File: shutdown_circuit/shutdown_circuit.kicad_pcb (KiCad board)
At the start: 2 copper layers, 36.8 x 25.8 mm, 21 parts, among them J1 SFTY, M3 Mounting_Hole, U1 AP111750, U2 74HC20D, U3 BTS6133D, m3 Mounting_Hole

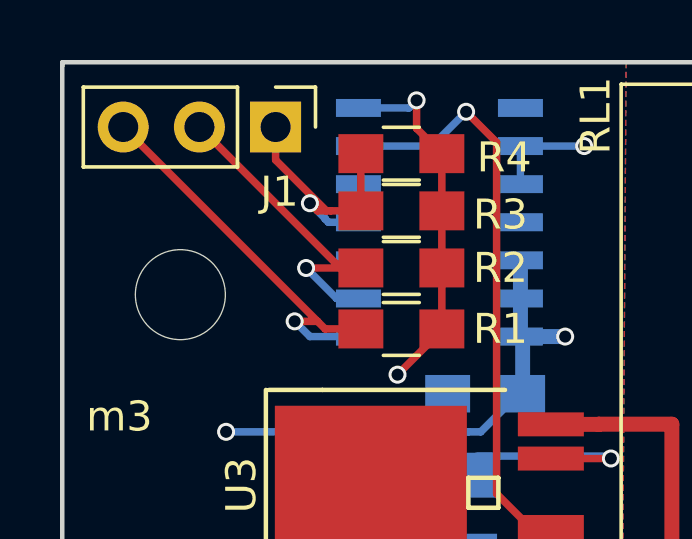
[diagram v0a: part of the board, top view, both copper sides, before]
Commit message: Move trace to avoid screw head
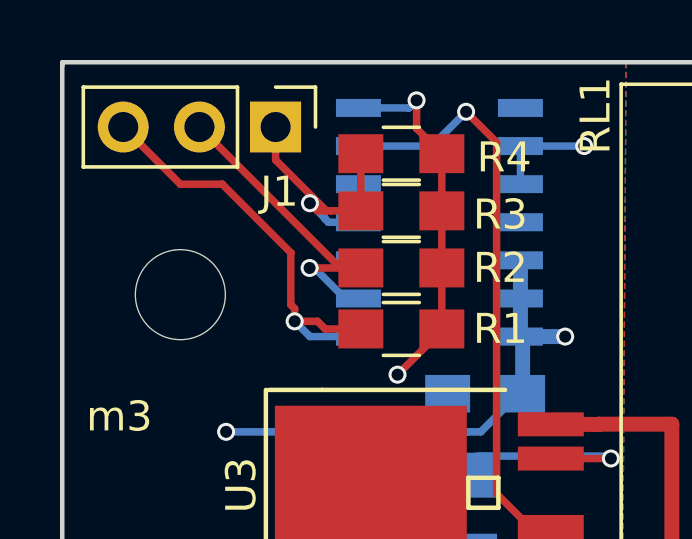
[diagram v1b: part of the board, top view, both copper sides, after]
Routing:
- net /IMD_Latched_Out: track 13.8 -> 14.3 mm
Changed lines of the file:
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@@
     (links 39)
     (no_connects 3)
-    (area 175.438999 118.288999 212.419001 144.220001)
+    (area 173.846238 117.348 214.519763 146.49)
     (thickness 1.6)
     (drawings 6)
-    (tracks 88)
+    (tracks 94)
     (zones 0)
     (modules 21)
@@
   (segment (start 184.32 123.317) (end 184.467 123.317) (width 0.25) (layer F.Cu) (net 6))
   (segment (start 184.467 123.317) (end 185.467 123.317) (width 0.25) (layer F.Cu) (net 6))
-  (segment (start 183.642 125.222) (end 184.658 126.238) (width 0.25) (layer B.Cu) (net 7))
-  (segment (start 184.658 126.238) (end 185.387 126.238) (width 0.25) (layer B.Cu) (net 7))
-  (segment (start 185.467 125.222) (end 183.642 125.222) (width 0.25) (layer F.Cu) (net 7))
-  (via (at 183.642 125.222) (size 0.6) (drill 0.4) (layers F.Cu B.Cu) (net 7))
+  (segment (start 183.921 125.222) (end 183.75901 125.222) (width 0.25) (layer B.Cu) (net 7))
+  (segment (start 185.387 126.238) (end 184.937 126.238) (width 0.25) (layer B.Cu) (net 7))
+  (segment (start 185.467 125.222) (end 183.75901 125.222) (width 0.25) (layer F.Cu) (net 7))
+  (via (at 183.75901 125.222) (size 0.6) (drill 0.4) (layers F.Cu B.Cu) (net 7))
+  (segment (start 184.937 126.238) (end 183.921 125.222) (width 0.25) (layer B.Cu) (net 7))
   (segment (start 180.086 120.523) (end 184.785 125.222) (width 0.25) (layer F.Cu) (net 7))
   (segment (start 184.785 125.222) (end 185.467 125.222) (width 0.25) (layer F.Cu) (net 7))
+  (segment (start 183.134 124.714) (end 183.134 126.448736) (width 0.25) (layer F.Cu) (net 8))
+  (segment (start 183.134 126.448736) (end 183.261 126.575736) (width 0.25) (layer F.Cu) (net 8))
+  (segment (start 183.261 126.575736) (end 183.261 127) (width 0.25) (layer F.Cu) (net 8))
+  (segment (start 180.848 122.428) (end 183.134 124.714) (width 0.25) (layer F.Cu) (net 8))
+  (segment (start 179.451 122.428) (end 180.848 122.428) (width 0.25) (layer F.Cu) (net 8))
+  (segment (start 177.546 120.523) (end 179.451 122.428) (width 0.25) (layer F.Cu) (net 8))
   (segment (start 183.769 127.508) (end 185.387 127.508) (width 0.25) (layer B.Cu) (net 8))
   (segment (start 183.261 127) (end 183.769 127.508) (width 0.25) (layer B.Cu) (net 8))
   (segment (start 184.023 127) (end 184.277 127.254) (width 0.25) (layer F.Cu) (net 8))
-  (segment (start 177.546 120.523) (end 184.023 127) (width 0.25) (layer F.Cu) (net 8))
   (segment (start 184.023 127) (end 183.261 127) (width 0.25) (layer F.Cu) (net 8))
   (via (at 183.261 127) (size 0.6) (drill 0.4) (layers F.Cu B.Cu) (net 8))
